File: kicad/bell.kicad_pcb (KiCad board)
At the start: 2 copper layers, 11 parts, among them IC1 ATTINY13A-SS, Q1 BD136

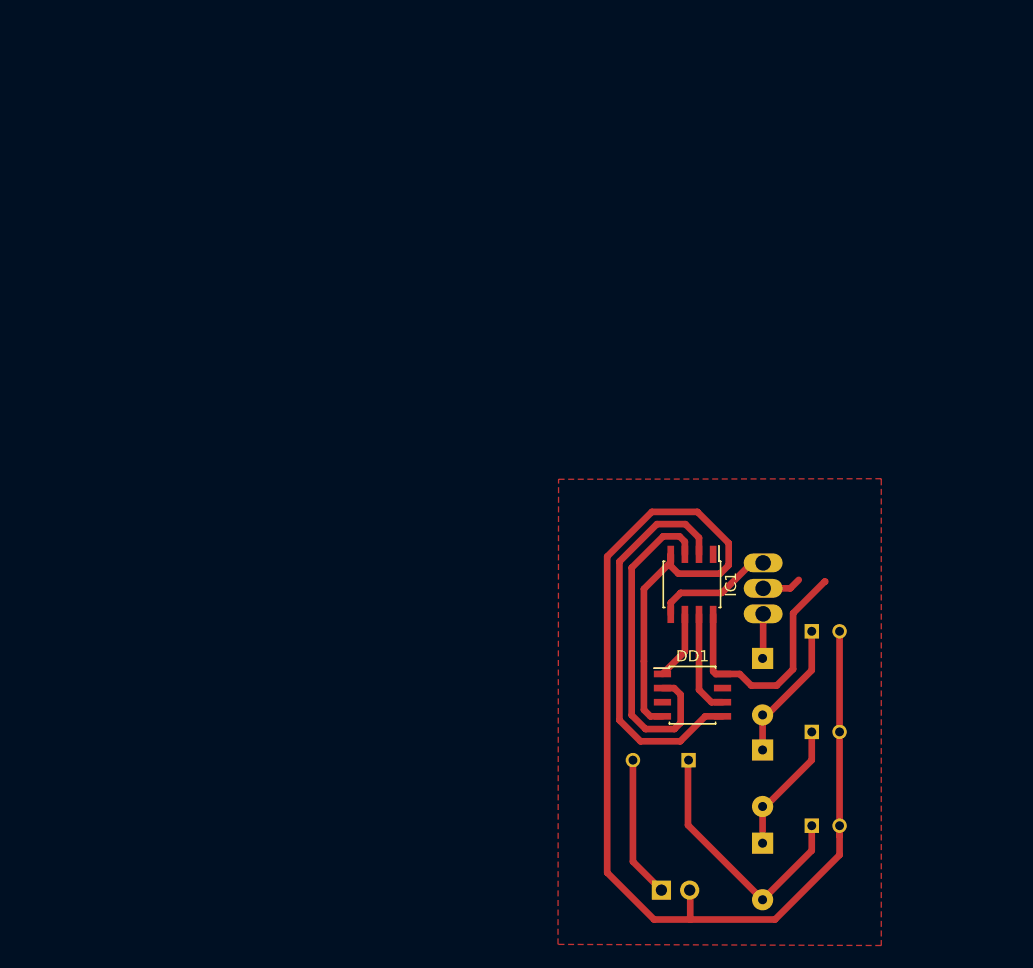
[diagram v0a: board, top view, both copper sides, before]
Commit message: Add board
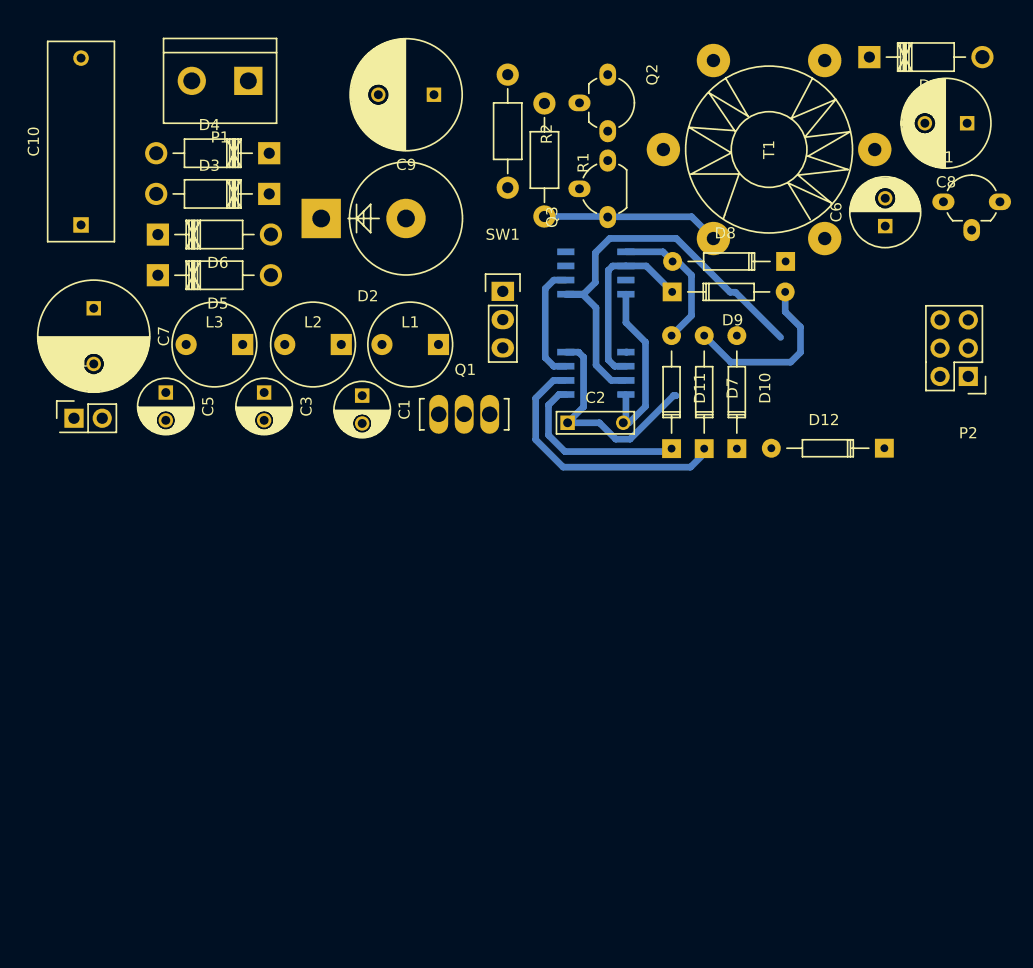
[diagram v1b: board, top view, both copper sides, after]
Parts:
- removed C4: CP1, Capacitors_ThroughHole:C_Radial_D10_L16_P5
- added C10: C, Capacitors_ThroughHole:C_Rect_L18_W6_P15, F.Cu at (44.9, 37.8)
- added C5: CP1, Capacitors_ThroughHole:C_Radial_D5_L11_P2.5, F.Cu at (52.5, 52.9)
- added C6: CP1, Capacitors_ThroughHole:C_Radial_D6.3_L11.2_P2.5, F.Cu at (117.2, 37.9)
- added C7: CP1, Capacitors_ThroughHole:C_Radial_D10_L16_P5, F.Cu at (46.1, 45.3)
- added C8: CP1, Capacitors_ThroughHole:C_Radial_D8_L13_P3.8, F.Cu at (124.6, 28.7)
- added C9: CP1, Capacitors_ThroughHole:C_Radial_D10_L21_P5, F.Cu at (76.6, 26.1)
- added D1: DIODESCH, Diodes_ThroughHole:Diode_DO-41_SOD81_Horizontal_RM10, F.Cu at (115.8, 22.8)
- added D10: DIODE, Diodes_ThroughHole:Diode_DO-35_SOD27_Horizontal_RM10, F.Cu at (103.9, 58.0)
- added D11: DIODE, Diodes_ThroughHole:Diode_DO-35_SOD27_Horizontal_RM10, F.Cu at (98.0, 58.0)
- added D12: DIODE, Diodes_ThroughHole:Diode_DO-35_SOD27_Horizontal_RM10, F.Cu at (117.1, 57.9)
- added D2: ZENER, Diodes_ThroughHole:Diode_P600_Vertical_KathodeUp, F.Cu at (66.5, 37.3)
- added D3: DIODE, Diodes_ThroughHole:Diode_DO-41_SOD81_Horizontal_RM10, F.Cu at (61.8, 35.1)
- added D4: DIODE, Diodes_ThroughHole:Diode_DO-41_SOD81_Horizontal_RM10, F.Cu at (61.8, 31.4)
- added D5: DIODE, Diodes_ThroughHole:Diode_DO-41_SOD81_Horizontal_RM10, F.Cu at (51.8, 42.4)
- added D6: DIODE, Diodes_ThroughHole:Diode_DO-41_SOD81_Horizontal_RM10, F.Cu at (51.8, 38.7)
- added D7: DIODE, Diodes_ThroughHole:Diode_DO-35_SOD27_Horizontal_RM10, F.Cu at (100.9, 58.0)
- added D8: DIODE, Diodes_ThroughHole:Diode_DO-35_SOD27_Horizontal_RM10, F.Cu at (108.2, 41.1)
- added D9: DIODE, Diodes_ThroughHole:Diode_DO-35_SOD27_Horizontal_RM10, F.Cu at (98.0, 43.9)
- added P1: CONN_2, Connect:bornier2, F.Cu at (57.4, 24.9)
- added P2: CONN_3X2, Pin_Headers:Pin_Header_Straight_2x03, F.Cu at (124.7, 51.5)
- added Q2: BC556, TO_SOT_Packages_THT:TO-92_Molded_Wide_Oval_Reverse, F.Cu at (92.3, 24.3)
- added Q3: BC556, TO_SOT_Packages_THT:TO-92_Molded_Wide_Oval, F.Cu at (92.3, 37.1)
- added R1: R, Resistors_ThroughHole:Resistor_Horizontal_RM10mm, F.Cu at (86.6, 26.9)
- added R2: R, Resistors_ThroughHole:Resistor_Horizontal_RM10mm, F.Cu at (83.3, 24.3)
- added SW1: SWITCH_INV, Pin_Headers:Pin_Header_Straight_1x03, F.Cu at (82.8, 43.8)
- added T1: TRANSFO4, Choke_Toroid_ThroughHole:Transformer_Toroid_Tapped_Horizontal_Diameter14mm_Amidon-T50, F.Cu at (106.8, 31.1)
- added U1: NCP1117ST33T3G, TO_SOT_Packages_THT:TO-92_Molded_Wide_Oval_Reverse, F.Cu at (122.4, 35.8)
- C1, C3, L1, L2, L3, SP1: moved to F.Cu
- C2: value CP1 -> C; footprint Capacitors_ThroughHole:C_Radial_D5_L11_P2.5 -> Capacitors_ThroughHole:C_Rect_L7_W2_P5; moved to F.Cu
- DD1, IC1: moved to B.Cu
- Q1: value BD136 -> BD137; moved to F.Cu
- moved L3 68.4 mm to (56.9, 48.6), turned to 180 degrees
- moved SP1 67.7 mm to (44.3, 55.2)
- moved C3 62.8 mm to (61.4, 52.9), turned to 270 degrees
- moved L2 56.2 mm to (65.8, 48.6), turned to 180 degrees
- moved C1 45.6 mm to (70.2, 53.2), turned to 270 degrees
- moved L1 44.2 mm to (74.5, 48.6), turned to 180 degrees
- moved DD1 38.9 mm to (91.2, 42.2), turned to 180 degrees
- moved C2 35.4 mm to (88.6, 55.6)
- moved Q1 31.1 mm to (79.3, 54.9), turned to 0 degrees
- moved IC1 20.8 mm to (91.2, 51.2), turned to 180 degrees
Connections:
- DD1 pad 1: Net-(DD1-Pad1) -> Net-(D11-Pad2)
- DD1 pad 2: Net-(DD1-Pad2) -> Net-(D9-Pad1)
- DD1 pad 4: (no net) -> GNDPWR
- DD1 pad 5: Net-(DD1-Pad5) -> Net-(D10-Pad2)
- DD1 pad 8: (no net) -> Net-(DD1-Pad8)
- IC1 pad 1: (no net) -> Net-(D8-Pad1)
- IC1 pad 2: Net-(DD1-Pad5) -> Net-(D9-Pad1)
- IC1 pad 3: Net-(DD1-Pad2) -> Net-(D10-Pad2)
- IC1 pad 5: Net-(IC1-Pad5) -> Net-(D11-Pad1)
- IC1 pad 6: Net-(DD1-Pad1) -> Net-(D7-Pad1)
- IC1 pad 8: (no net) -> Net-(C2-Pad1)
- L2 pad 2: Net-(C2-Pad1) -> Net-(C3-Pad1)
- L3 pad 1: Net-(C2-Pad1) -> Net-(C3-Pad1)
- L3 pad 2: Net-(C3-Pad1) -> Net-(C5-Pad1)
- Q1 pad 2: (no net) -> +12V
- Q1 pad 3: Net-(IC1-Pad5) -> Net-(D7-Pad1)
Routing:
- net GNDPWR: track 116.6 -> 16.1 mm
- net Net-(D10-Pad2): track 0.00 -> 38.3 mm
- net Net-(DD1-Pad5): track 35.8 -> 0.00 mm
- net Net-(DD1-Pad2): track 30.1 -> 0.00 mm
- net (no net): track 26.1 -> 0.00 mm
- net Net-(D7-Pad1): track 0.00 -> 24.2 mm
- net Net-(C3-Pad1): track 23.8 -> 0.00 mm
- net Net-(D11-Pad1): track 0.00 -> 16.9 mm
- net Net-(D9-Pad1): track 0.00 -> 16.7 mm
- net Net-(Q3-Pad1): track 0.00 -> 16.0 mm
- net Net-(D7-Pad2): track 0.00 -> 16.0 mm
- net Net-(D11-Pad2): track 0.00 -> 12.9 mm
- net Net-(C7-Pad2): track 12.7 -> 0.00 mm
- net Net-(C1-Pad1): track 12.7 -> 0.00 mm
- net Net-(IC1-Pad5): track 10.8 -> 0.00 mm
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- removed copper zone on F.Cu, net GNDPWR

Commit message: New
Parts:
- added C4: C, Capacitors_ThroughHole:C_Rect_L7_W2_P5, F.Cu at (88.3, 39.7)
- added D13: DIODESCH, Diodes_ThroughHole:Diode_DO-41_SOD81_Horizontal_RM10, F.Cu at (114.9, 37.8)
- DD1: footprint Housings_SOIC:SOIC-8_3.9x4.9mm_Pitch1.27mm -> Housings_SOIC:SOIJ-8_5.3x5.3mm_Pitch1.27mm
- T1: value TRANSFO4 -> TRANSFO_4
- U1: value NCP1117ST33T3G -> LM7805CT; footprint TO_SOT_Packages_THT:TO-92_Molded_Wide_Oval_Reverse -> TO_SOT_Packages_THT:TO-92_Molded_Wide_Oval
- moved C5 16.9 mm to (65.1, 41.6), turned to 90 degrees
- moved C3 16.8 mm to (76.5, 45.4), turned to 90 degrees
- moved C7 15.6 mm to (61.6, 45.4), turned to 180 degrees
- moved D2 15.1 mm to (80.2, 43.8), turned to 90 degrees
- moved C10 13.4 mm to (58.3, 38.5)
- moved D5 13.0 mm to (63.3, 36.1)
- moved L3 13.0 mm to (69.5, 45.3)
- moved SP1 12.9 mm to (57.0, 53.2)
- moved D6 12.7 mm to (63.3, 33.2)
- moved D3 12.5 mm to (73.4, 30.3)
- moved D4 12.3 mm to (73.4, 27.2)
- moved P1 12.1 mm to (69.4, 23.5)
- moved D7 11.9 mm to (95.7, 47.2), turned to 0 degrees
- moved D8 11.7 mm to (100.5, 49.8), turned to 0 degrees
- moved C1 9.28 mm to (78.5, 49.1), turned to 0 degrees
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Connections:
- C8 pad 1: +12V -> Net-(C8-Pad1)
- D1 pad 2: +12V -> Net-(C8-Pad1)
- Q1 pad 2: +12V -> (no net)
- T1 pad 4: GNDPWR -> Net-(D1-Pad1)
- T1 pad 5: Net-(D1-Pad1) -> GNDPWR
- T1 pad 6: (no net) -> Net-(D13-Pad1)
- U1 pad 1: GNDPWR -> Net-(C8-Pad1)
- U1 pad 2: VDD -> GNDPWR
- U1 pad 3: +12V -> VDD
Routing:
- net Net-(D10-Pad2): track 38.3 -> 0.00 mm
- net Net-(D7-Pad1): track 24.2 -> 0.00 mm
- net Net-(C2-Pad1): track 20.4 -> 0.00 mm
- net Net-(D11-Pad1): track 16.9 -> 0.00 mm
- net Net-(D9-Pad1): track 16.7 -> 0.00 mm
- net GNDPWR: track 16.1 -> 0.00 mm
- net Net-(Q3-Pad1): track 16.0 -> 0.00 mm
- net Net-(D7-Pad2): track 16.0 -> 0.00 mm
- net Net-(D11-Pad2): track 12.9 -> 0.00 mm
- net Net-(DD1-Pad6): track 10.5 -> 0.00 mm

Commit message: Board
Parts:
- added R3: R, Resistors_ThroughHole:Resistor_Horizontal_RM10mm, F.Cu at (101.5, 41.9)
- moved C4 9.70 mm to (88.8, 49.4)
- moved DD1 9.45 mm to (96.8, 51.3)
- moved IC1 9.24 mm to (96.4, 42.6)
- moved C2 8.88 mm to (88.5, 40.7)
- moved D10 8.03 mm to (118.4, 50.6)
- moved D7 7.96 mm to (93.9, 55.0)
- moved D8 7.94 mm to (108.3, 48.4)
- moved D11 7.46 mm to (92.0, 47.8)
- moved D1 3.80 mm to (114.9, 25.4)
- moved SP1 3.40 mm to (59.9, 54.9), turned to 90 degrees
- moved SW1 3.34 mm to (84.2, 47.6), turned to 180 degrees
- moved D12 3.00 mm to (118.2, 54.9)
- moved C8 2.30 mm to (124.4, 31.9)
- moved D9 0.64 mm to (97.7, 46.2)
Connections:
- net Net-(C8-Pad1) renamed +5V
- Q1 pad 1: Net-(L1-Pad1) -> GNDPWR
- Q1 pad 2: (no net) -> Net-(L1-Pad1)
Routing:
- net GNDPWR: track 0.00 -> 157.6 mm, vias 0 -> 1
- net Net-(C9-Pad2): track 0.00 -> 51.6 mm
- net +5V: track 0.00 -> 48.3 mm
- net VDD: track 0.00 -> 47.9 mm
- net Net-(DD1-Pad6): track 0.00 -> 45.4 mm, vias 0 -> 1
- net Net-(C9-Pad1): track 0.00 -> 43.2 mm
- net Net-(D8-Pad1): track 0.00 -> 32.5 mm
- net Net-(D10-Pad2): track 0.00 -> 29.9 mm
- net Net-(D7-Pad2): track 0.00 -> 29.6 mm
- net Net-(D7-Pad1): track 0.00 -> 26.3 mm
- net Net-(L1-Pad1): track 0.00 -> 25.3 mm
- net Net-(D11-Pad2): track 0.00 -> 24.9 mm
- net Net-(D11-Pad1): track 0.00 -> 24.7 mm
- net Net-(D4-Pad2): track 0.00 -> 21.8 mm
- net Net-(D10-Pad1): track 0.00 -> 17.3 mm
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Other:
- board outline added: 71.1 x 37 mm

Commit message: New
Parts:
- removed D10, D11, D12, D7, D8, D9: DIODE, Diodes_ThroughHole:Diode_DO-35_SOD27_Horizontal_RM10
- removed R3: R, Resistors_ThroughHole:Resistor_Horizontal_RM10mm
- moved P2 7.53 mm to (113.8, 49.1)
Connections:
- DD1 pad 1: Net-(D11-Pad2) -> Net-(DD1-Pad1)
- DD1 pad 2: Net-(D9-Pad1) -> Net-(DD1-Pad2)
- DD1 pad 5: Net-(D10-Pad2) -> Net-(DD1-Pad5)
- IC1 pad 1: Net-(D8-Pad1) -> (no net)
- IC1 pad 2: Net-(D9-Pad1) -> Net-(DD1-Pad5)
- IC1 pad 3: Net-(D10-Pad2) -> Net-(DD1-Pad2)
- IC1 pad 5: Net-(D11-Pad1) -> Net-(IC1-Pad5)
- IC1 pad 6: Net-(D7-Pad1) -> Net-(DD1-Pad1)
- P2 pad 1: Net-(D7-Pad2) -> Net-(DD1-Pad2)
- P2 pad 4: Net-(D10-Pad1) -> Net-(DD1-Pad5)
- P2 pad 5: Net-(D8-Pad1) -> Net-(DD1-Pad1)
- Q1 pad 1: GNDPWR -> Net-(L1-Pad1)
- Q1 pad 2: Net-(L1-Pad1) -> (no net)
- Q1 pad 3: Net-(D7-Pad1) -> Net-(IC1-Pad5)
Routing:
- net GNDPWR: track 157.6 -> 81.3 mm, vias 1 -> 0
- net VDD: track 47.9 -> 5.10 mm
- net Net-(D8-Pad1): track 32.5 -> 0.00 mm
- net Net-(DD1-Pad6): track 45.4 -> 13.1 mm, vias 1 -> 0
- net Net-(D10-Pad2): track 29.9 -> 0.00 mm
- net Net-(D7-Pad2): track 29.6 -> 0.00 mm
- net Net-(D7-Pad1): track 26.3 -> 0.00 mm
- net Net-(D11-Pad2): track 24.9 -> 0.00 mm
- net Net-(D11-Pad1): track 24.7 -> 0.00 mm
- net +5V: track 48.3 -> 23.8 mm
- net Net-(L1-Pad1): track 25.3 -> 1.40 mm
- net Net-(DD1-Pad2): track 0.00 -> 21.5 mm
- net Net-(D10-Pad1): track 17.3 -> 0.00 mm
- net Net-(DD1-Pad5): track 0.00 -> 16.0 mm
- net Net-(D9-Pad1): track 12.8 -> 0.00 mm
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
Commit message: Fix
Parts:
- removed IC1: ATTINY13A-SS, Housings_SOIC:SOIC-8_3.9x4.9mm_Pitch1.27mm
- added DD2: w25q64fvssig, Housings_SOIC:SOIJ-8_5.3x5.3mm_Pitch1.27mm, B.Cu at (109.8, 48.9)
- added R3: 5.1, Resistors_ThroughHole:Resistor_Horizontal_RM10mm, F.Cu at (114.6, 43.8)
- C1: value CP1 -> 2.2
- C10: value C -> 2.2
- C2, C4: value C -> 0.1; footprint Capacitors_ThroughHole:C_Rect_L7_W2_P5 -> cymometer:C_Rect_L10_W2.5_P5
- C3, C5: value CP1 -> 1.0
- C6: value CP1 -> 10.0
- C7: value CP1 -> 100.0
- C8: value CP1 -> 470.0
- C9: value CP1 -> 22.0
- D2: value ZENER -> Д816Г
- D3, D4, D5, D6: value DIODE -> 1N4007
- DD1: value w25q64fvssig -> ATTINY13A-SS; footprint Housings_SOIC:SOIJ-8_5.3x5.3mm_Pitch1.27mm -> Housings_SOIC:SOIC-8_3.9x4.9mm_Pitch1.27mm
- L1: value INDUCTOR -> 150 uH
- L2, L3: value INDUCTOR -> 20 uH
- Q2, Q3: value BC556 -> КТ313
- R1, R2: value R -> 5.1 k
- T1: footprint Choke_Toroid_ThroughHole:Transformer_Toroid_Tapped_Horizontal_Diameter14mm_Amidon-T50 -> Choke_Toroid_ThroughHole:Transformer_Toroid_Tapped_horizontal_Diameter9mm_Amidon-T30
- moved L2 23.4 mm to (87.1, 43.1), turned to 90 degrees
- moved SW1 21.8 mm to (104.1, 38.7), turned to 270 degrees
- moved C10 18.5 mm to (76.4, 42.6), turned to 180 degrees
- moved C3 18.5 mm to (93.9, 39.4), turned to 270 degrees
- moved C5 17.6 mm to (81.6, 47.7), turned to 0 degrees
- moved C4 17.5 mm to (106.3, 48.9), turned to 90 degrees
- moved C1 15.6 mm to (94.1, 47.7), turned to 90 degrees
- moved C2 14.2 mm to (102.5, 43.2), turned to 0 degrees
- moved L1 13.7 mm to (87.1, 52.9), turned to 90 degrees
- moved Q1 11.9 mm to (94.1, 53.5), turned to 90 degrees
- moved L3 11.9 mm to (78.7, 53.0)
- moved C7 11.7 mm to (72.0, 50.7)
- moved C8 6.34 mm to (119.0, 28.4)
- moved D13 5.87 mm to (110.4, 34.0)
- moved U1 5.81 mm to (120.5, 37.3)
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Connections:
- DD1 pad 1: Net-(DD1-Pad1) -> (no net)
- DD1 pad 3: (no net) -> Net-(DD1-Pad3)
- DD1 pad 7: (no net) -> Net-(DD1-Pad7)
- DD1 pad 8: Net-(C4-Pad1) -> Net-(C2-Pad1)
- P2 pad 1: Net-(DD1-Pad2) -> Net-(DD1-Pad3)
- P2 pad 3: Net-(DD1-Pad6) -> Net-(DD1-Pad7)
- P2 pad 4: Net-(DD1-Pad5) -> Net-(DD1-Pad2)
- P2 pad 5: Net-(DD1-Pad1) -> Net-(DD1-Pad6)
- Q1 pad 1: Net-(L1-Pad1) -> GNDPWR
- Q1 pad 2: (no net) -> Net-(L1-Pad1)
- Q1 pad 3: Net-(IC1-Pad5) -> Net-(DD1-Pad5)
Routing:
- net GNDPWR: track 81.3 -> 142.9 mm
- net Net-(DD1-Pad6): track 13.1 -> 52.5 mm
- net Net-(L1-Pad1): track 1.40 -> 30.9 mm
- net Net-(DD1-Pad3): track 0.00 -> 26.6 mm
- net Net-(DD1-Pad7): track 0.00 -> 25.0 mm
- net VDD: track 5.10 -> 27.7 mm
- net Net-(C9-Pad2): track 51.6 -> 68.4 mm
- net Net-(C10-Pad2): track 8.58 -> 24.0 mm
- net Net-(DD1-Pad2): track 21.5 -> 35.9 mm, vias 0 -> 1
- net Net-(C4-Pad1): track 4.27 -> 18.4 mm
- net Net-(C3-Pad1): track 16.3 -> 30.2 mm
- net Net-(C10-Pad1): track 10.8 -> 21.5 mm
- net Net-(C5-Pad1): track 9.93 -> 19.1 mm
- net Net-(C2-Pad1): track 5.68 -> 14.8 mm
- net +5V: track 23.8 -> 31.8 mm
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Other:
- board size 71.1 x 37 mm -> 63.6 x 37 mm

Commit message: Fix
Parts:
- R3: footprint Resistors_ThroughHole:Resistor_Horizontal_RM10mm -> Resistors_ThroughHole:Resistor_Horizontal_RM20mm
- moved R3 11.8 mm to (117.3, 55.3), turned to 180 degrees
- moved P2 1.21 mm to (117.0, 46.0)
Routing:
- net Net-(L1-Pad1): track 30.9 -> 11.8 mm
- net +5V: track 31.8 -> 37.3 mm
- net Net-(DD1-Pad6): track 52.5 -> 49.6 mm
- net VDD: track 27.7 -> 26.2 mm
- net GNDPWR: track 142.9 -> 141.8 mm
- net Net-(DD1-Pad3): track 26.6 -> 25.7 mm
- net Net-(DD1-Pad7): track 25.0 -> 24.3 mm

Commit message: Fix
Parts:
- moved R3 0.50 mm to (117.3, 54.8)
- moved DD1 0.46 mm to (101.0, 48.8)
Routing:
- net Net-(C2-Pad1): track 14.8 -> 13.6 mm
